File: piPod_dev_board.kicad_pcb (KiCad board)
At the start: 2 copper layers, 100 x 100 mm, 25 parts, among them J1 USB_C_Receptacle_USB2.0, J2 Micro_SD_Card_Det_Hirose_DM3AT, Q1 DMG9926UDM, Q2 AO3401A, U1 AP9101CK, U2 MCP73828, U3 RP400N501A

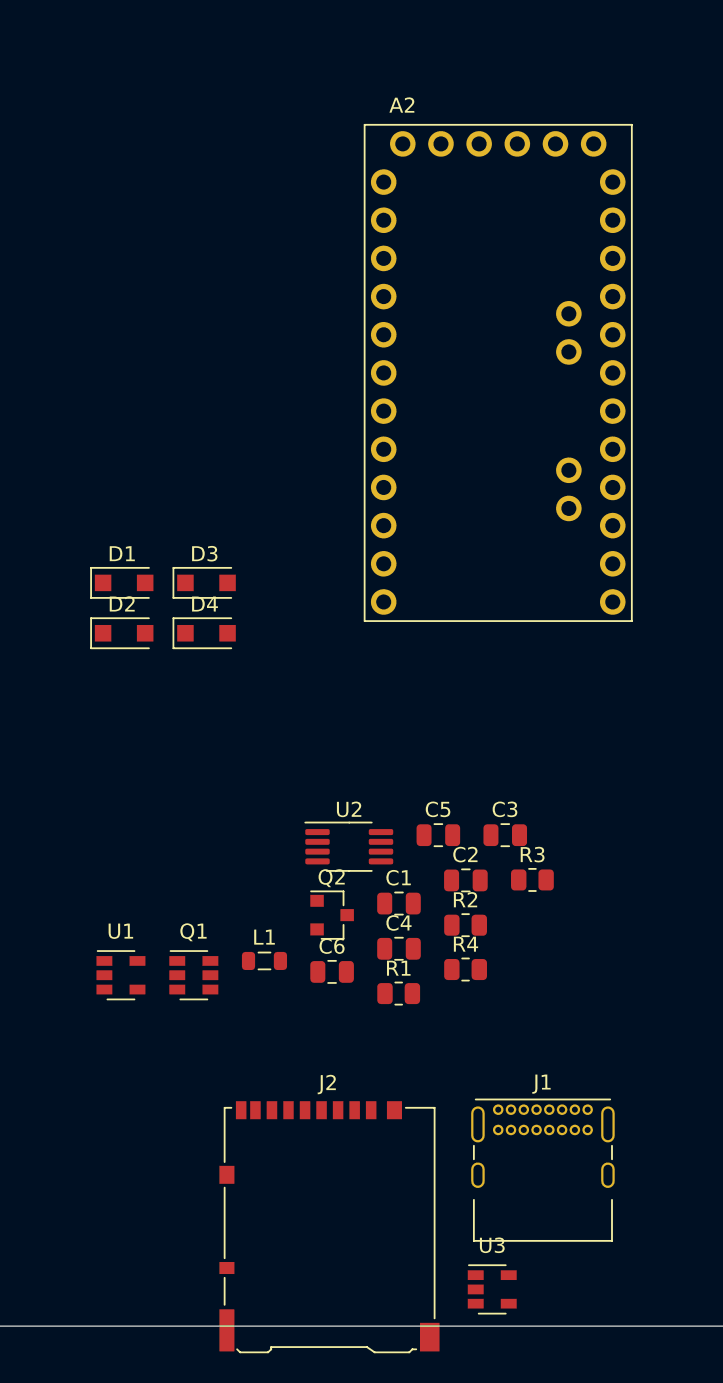
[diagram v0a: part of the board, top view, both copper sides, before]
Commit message: Redo power supply, switch to STM32 for SMC
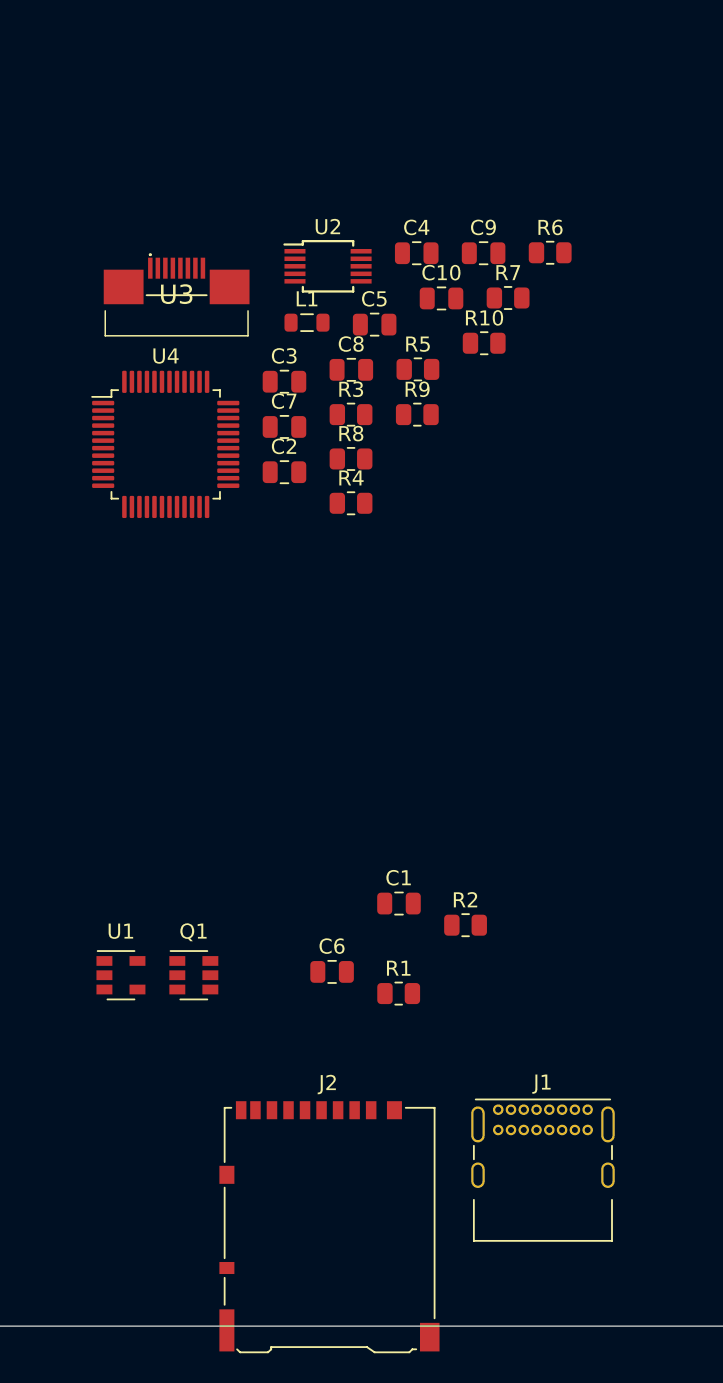
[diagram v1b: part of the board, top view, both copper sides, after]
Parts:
- removed A2: ARDUINO_PRO_MINI, Gigahawk:ARDUINO_PRO_MINI_THT
- removed D1, D2, D3, D4: PMEG2010AEH, Diode_SMD:D_SOD-123F
- removed Q2: AO3401A, Package_TO_SOT_SMD:SOT-23
- added C10: 100n, Capacitor_SMD:C_0805_2012Metric, F.Cu at (43.5, 31.6)
- added C7: 100n, Capacitor_SMD:C_0805_2012Metric, F.Cu at (33.0, 40.2)
- added C8: 100n, Capacitor_SMD:C_0805_2012Metric, F.Cu at (37.5, 36.4)
- added C9: 1u, Capacitor_SMD:C_0805_2012Metric, F.Cu at (46.3, 28.6)
- added R10: 10k, Resistor_SMD:R_0805_2012Metric, F.Cu at (46.3, 34.6)
- added R5: 300R, Resistor_SMD:R_0805_2012Metric, F.Cu at (41.9, 36.3)
- added R6: 2k, Resistor_SMD:R_0805_2012Metric, F.Cu at (50.7, 28.6)
- added R7: 1k54, Resistor_SMD:R_0805_2012Metric, F.Cu at (47.9, 31.6)
- added R8: 69k8, Resistor_SMD:R_0805_2012Metric, F.Cu at (37.5, 42.3)
- added R9: 10k, Resistor_SMD:R_0805_2012Metric, F.Cu at (41.9, 39.4)
- added U4: STM32L051C8Tx, Package_QFP:LQFP-48_7x7mm_P0.5mm, F.Cu at (25.1, 41.3)
- C2, C3, C4: value 10u -> 4u7
- C5: value 10u -> 100n
- L1: value L_Small -> 27n
- R3: value 100k -> 140R
- R4: value 100m -> 290R
- U2: value MCP73828 -> MCP73833-MSOP; footprint Package_SO:MSOP-8_3x3mm_P0.65mm -> Package_SO:MSOP-10_3x3mm_P0.5mm
- U3: value RP400N501A -> IPOD4_CW; footprint Package_TO_SOT_SMD:SOT-23-5 -> Gigahawk:SFV8R2STE1HLF
- moved U3 69.4 mm to (25.8, 31.4)
- moved C4 46.3 mm to (41.8, 28.6)
- moved L1 42.6 mm to (34.5, 33.2)
- moved U2 38.6 mm to (35.9, 29.5)
- moved C5 34.2 mm to (39.0, 33.4)
- moved C3 33.6 mm to (33.0, 37.2)
- moved R3 33.2 mm to (37.5, 39.4)
- moved R4 31.9 mm to (37.5, 45.2)
- moved C2 29.7 mm to (33.0, 43.2)
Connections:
- net +1V8 renamed Net-(A1-PadPP9)
- A1 pad 1: +3V3 -> Net-(A1-Pad1)
- A1 pad 17: +3V3 -> Net-(A1-Pad17)
- A1 pad 2: +5V -> Net-(A1-Pad2)
- A1 pad 3: Net-(A1-Pad3) -> I2C_SDA
- A1 pad 4: +5V -> Net-(A1-Pad4)
- A1 pad 5: Net-(A1-Pad5) -> I2C_SCL
- A1 pad PP8: +3V3 -> Net-(A1-PadPP8)
- C2 pad 1: Net-(C2-Pad1) -> VBUS
- C4 pad 1: Net-(C4-Pad1) -> +3V3
- C5 pad 1: +5V -> +3V3
- L1 pad 1: Net-(C4-Pad1) -> +3V3
- L1 pad 2: Net-(D4-Pad2) -> +3.3VA
- R3 pad 1: Net-(C2-Pad1) -> Net-(R3-Pad1)
- R3 pad 2: Net-(R3-Pad2) -> Net-(D1-Pad1)
- R4 pad 1: Net-(Q2-Pad2) -> Net-(R4-Pad1)
- R4 pad 2: Net-(C2-Pad1) -> Net-(D2-Pad1)
- U2 pad 1: Net-(R3-Pad2) -> VBUS
- U2 pad 2: GND -> VBUS
- U2 pad 3: THERM -> Net-(R3-Pad1)
- U2 pad 4: CD10 -> Net-(R4-Pad1)
- U2 pad 5: +BATT -> GND
- U2 pad 7: Net-(Q2-Pad2) -> Net-(R5-Pad1)
- U2 pad 8: Net-(C2-Pad1) -> Net-(R7-Pad2)
- U3 pad 1: Net-(C4-Pad1) -> +3V3
- U3 pad 2: GND -> CW_CLK
- U3 pad 3: Net-(C4-Pad1) -> Net-(R10-Pad2)
- U3 pad 4: +5V -> (no net)
- U3 pad 5: Net-(D4-Pad2) -> (no net)

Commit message: Switch RPi footprint to THT
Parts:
- A1: footprint Gigahawk:RASPI_ZERO_1_3_SMT_LOW_PROFILE -> Gigahawk:RASPI_ZERO_1_3_THT
